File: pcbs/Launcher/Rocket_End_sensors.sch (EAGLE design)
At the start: 9 parts, among them U1 ARDUINO-MEGAPRO-5V, X1 22-23-2051, X3 22-23-2041, X5 22-23-2101, X6 22-23-2101, X7 22-23-2101, X8 22-23-2031

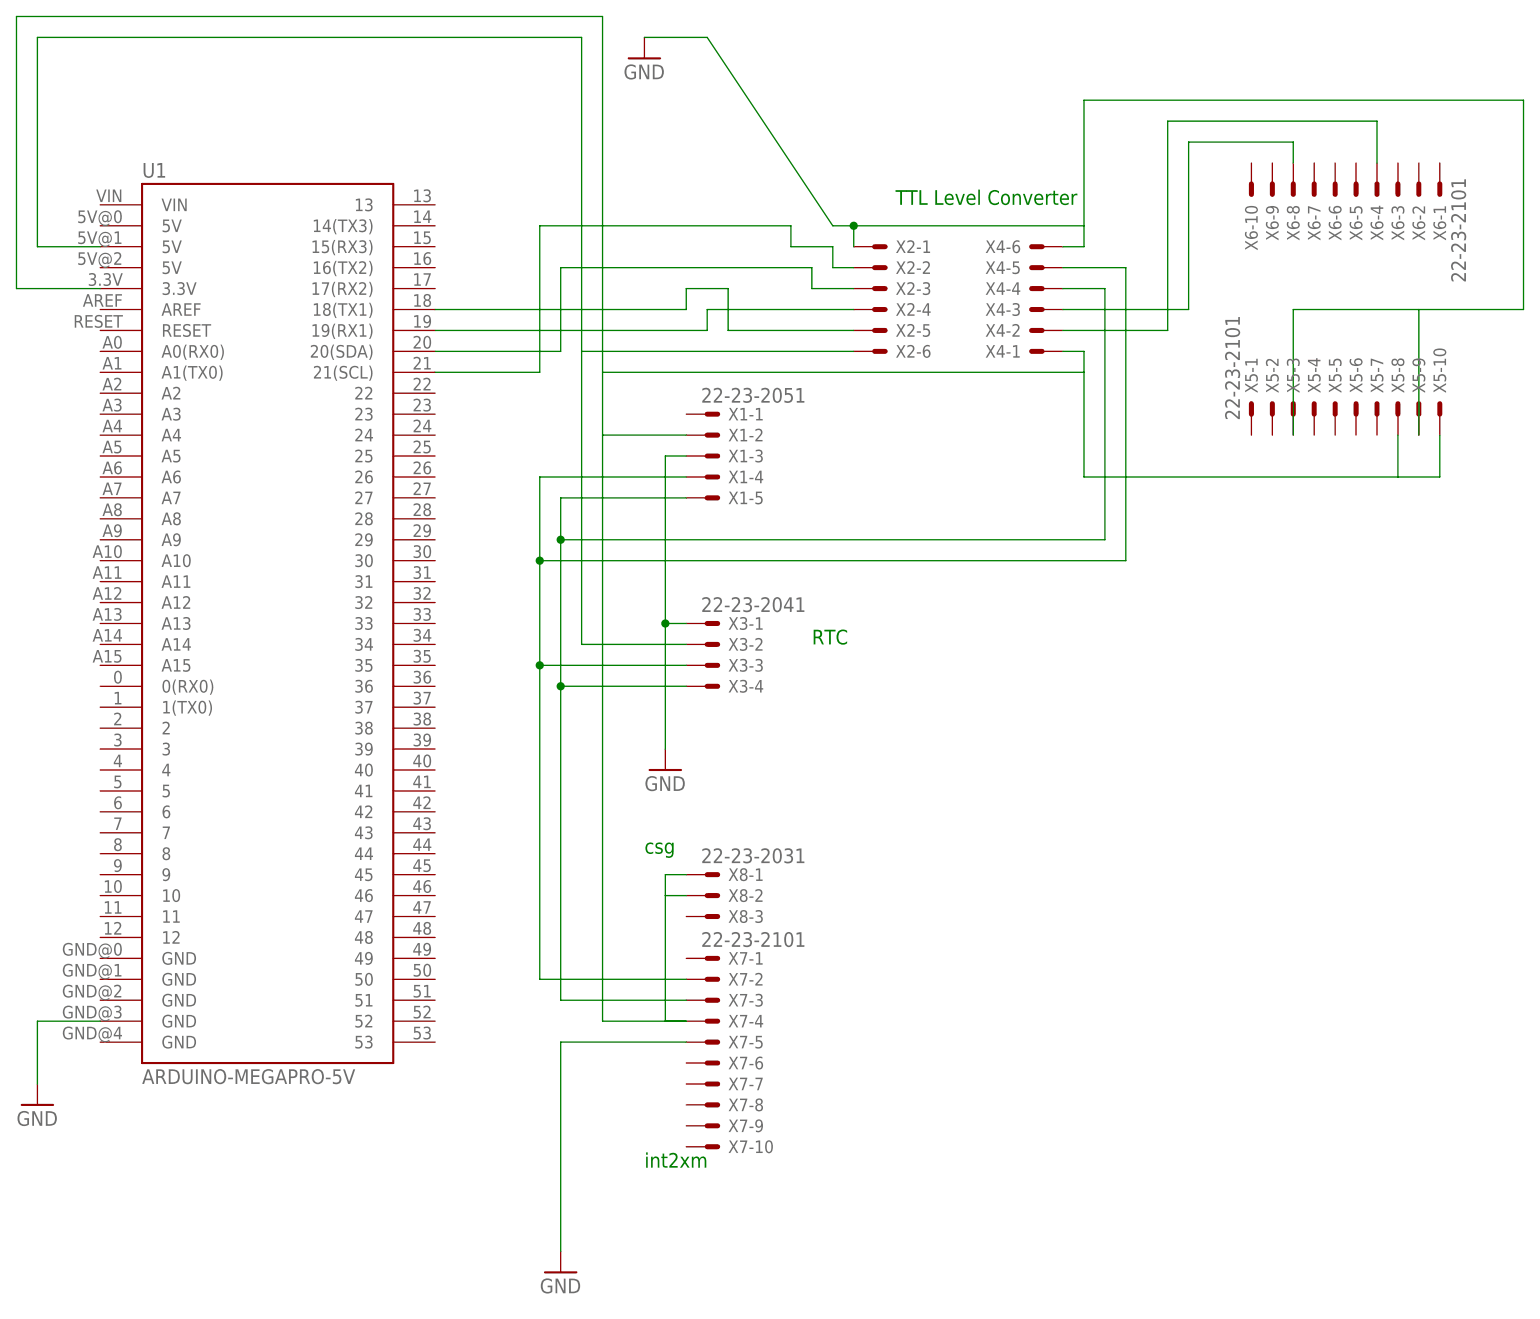
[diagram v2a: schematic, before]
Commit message: * More mods....fixed up gps wiring. * Making place where can run some wires underneath so don't need   two sides for relay board.
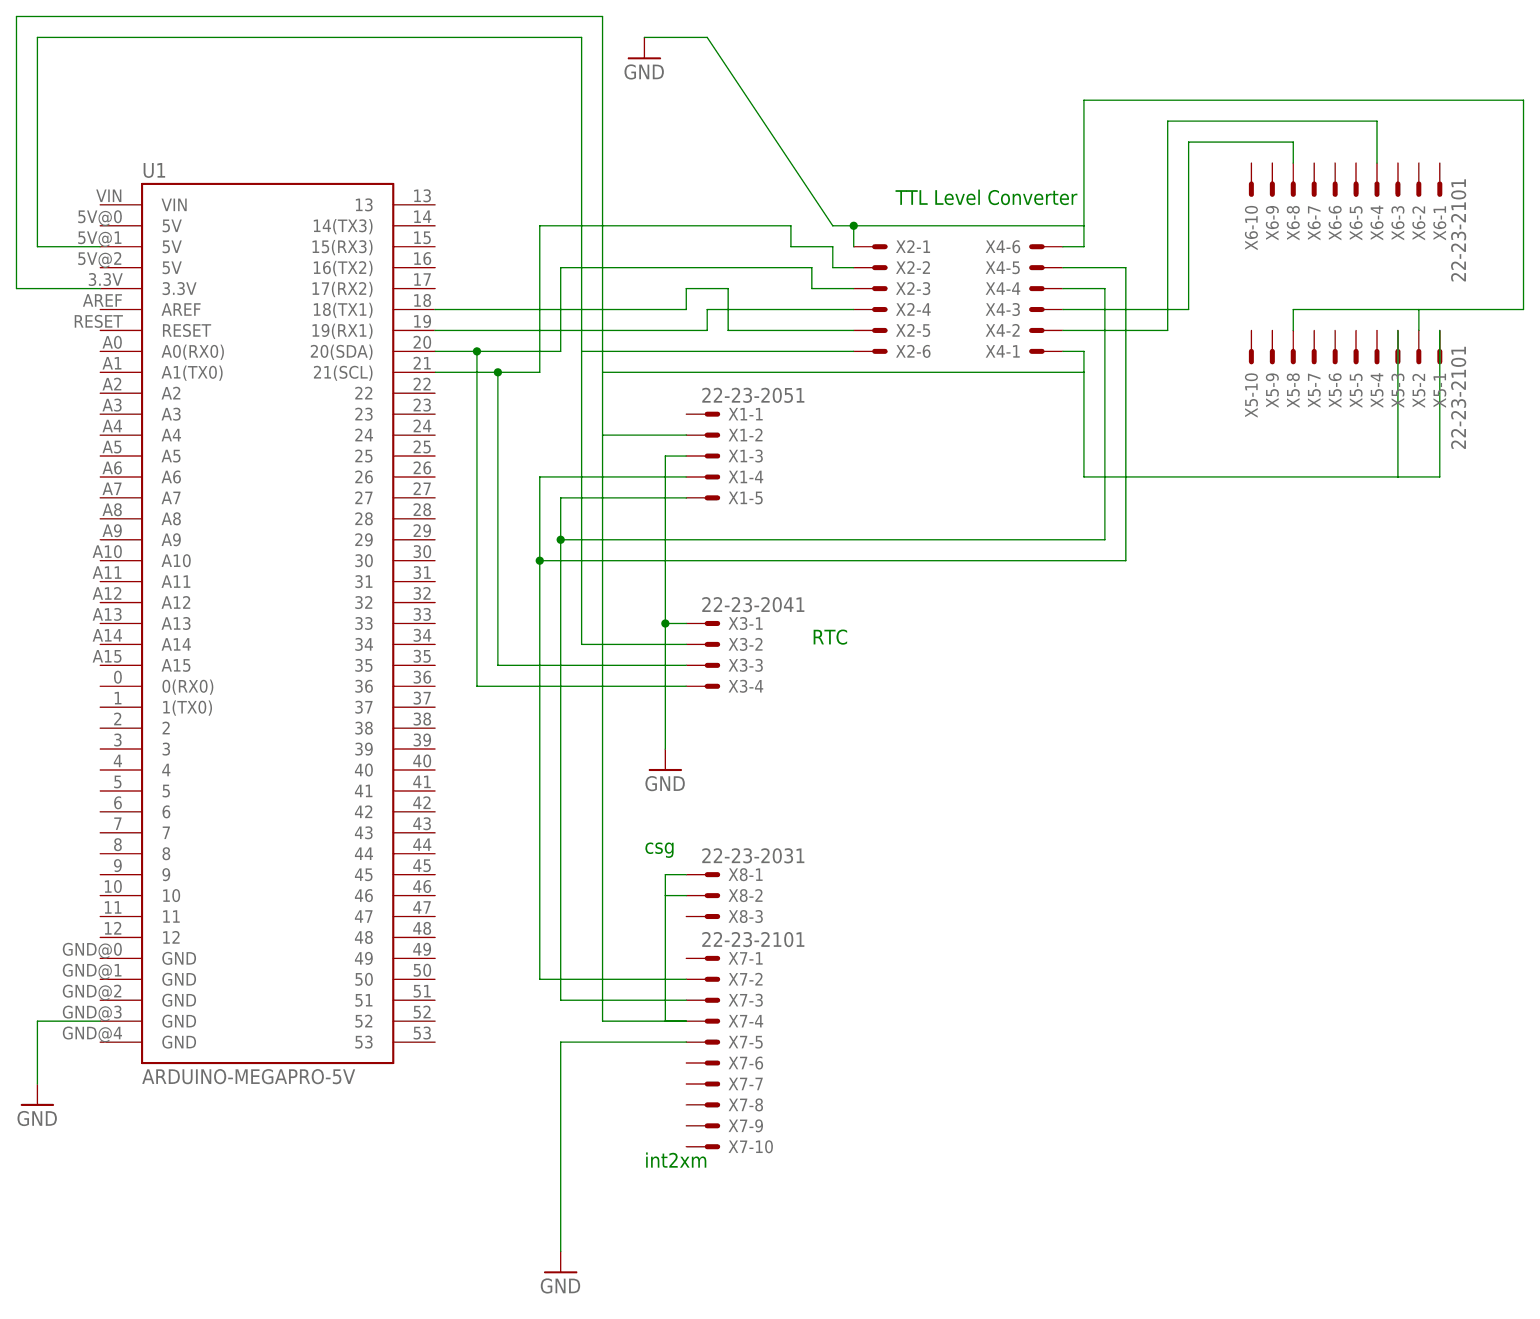
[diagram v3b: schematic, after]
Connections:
- net N$18: no longer X3-4.S
- net N$2: now also X3-3.S
- net N$24: no longer X3-3.S
- net N$4: now also X5-1.S, X5-3.S; no longer X5-10.S, X5-8.S
- net N$5: now also X3-4.S
- net N$7: now also X5-2.S, X5-8.S; no longer X5-3.S, X5-9.S
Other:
- moved on the sheet: X5-1, X5-10, X5-2, X5-3, X5-4, X5-5, X5-6, X5-7, X5-8, X5-9
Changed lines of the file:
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@@
 <part name="X4" library="con-molex" deviceset="22-23-2061" device=""/>
 <part name="GND2" library="supply1" deviceset="GND" device=""/>
-<part name="X5" library="con-molex" deviceset="22-23-2101" device=""/>
 <part name="X6" library="con-molex" deviceset="22-23-2101" device=""/>
 <part name="X7" library="con-molex" deviceset="22-23-2101" device=""/>
 <part name="X8" library="con-molex" deviceset="22-23-2031" device=""/>
 <part name="GND3" library="supply1" deviceset="GND" device=""/>
+<part name="X5" library="con-molex" deviceset="22-23-2101" device=""/>
 </parts>
 <sheets>
@@
 <instance part="X4" gate="-6" x="132.08" y="99.06" rot="R180"/>
 <instance part="GND2" gate="1" x="83.82" y="121.92"/>
-<instance part="X5" gate="-1" x="157.48" y="78.74" rot="R90"/>
-<instance part="X5" gate="-2" x="160.02" y="78.74" rot="R90"/>
-<instance part="X5" gate="-3" x="162.56" y="78.74" rot="R90"/>
-<instance part="X5" gate="-4" x="165.1" y="78.74" rot="R90"/>
-<instance part="X5" gate="-5" x="167.64" y="78.74" rot="R90"/>
-<instance part="X5" gate="-6" x="170.18" y="78.74" rot="R90"/>
-<instance part="X5" gate="-7" x="172.72" y="78.74" rot="R90"/>
-<instance part="X5" gate="-8" x="175.26" y="78.74" rot="R90"/>
-<instance part="X5" gate="-9" x="177.8" y="78.74" rot="R90"/>
-<instance part="X5" gate="-10" x="180.34" y="78.74" rot="R90"/>
 <instance part="X6" gate="-1" x="180.34" y="106.68" rot="R270"/>
 <instance part="X6" gate="-2" x="177.8" y="106.68" rot="R270"/>
@@
 <instance part="X8" gate="-3" x="91.44" y="17.78"/>
 <instance part="GND3" gate="1" x="73.66" y="-25.4"/>
+<instance part="X5" gate="-1" x="180.34" y="86.36" rot="R270"/>
+<instance part="X5" gate="-2" x="177.8" y="86.36" rot="R270"/>
+<instance part="X5" gate="-3" x="175.26" y="86.36" rot="R270"/>
+<instance part="X5" gate="-4" x="172.72" y="86.36" rot="R270"/>
+<instance part="X5" gate="-5" x="170.18" y="86.36" rot="R270"/>
+<instance part="X5" gate="-6" x="167.64" y="86.36" rot="R270"/>
+<instance part="X5" gate="-7" x="165.1" y="86.36" rot="R270"/>
+<instance part="X5" gate="-8" x="162.56" y="86.36" rot="R270"/>
+<instance part="X5" gate="-9" x="160.02" y="86.36" rot="R270"/>
+<instance part="X5" gate="-10" x="157.48" y="86.36" rot="R270"/>
 </instances>
 <busses>
@@
 <wire x1="88.9" y1="68.58" x2="73.66" y2="68.58" width="0.1524" layer="91"/>
 <pinref part="X7" gate="-3" pin="S"/>
-<wire x1="73.66" y1="63.5" x2="73.66" y2="45.72" width="0.1524" layer="91"/>
-<wire x1="73.66" y1="45.72" x2="73.66" y2="7.62" width="0.1524" layer="91"/>
+<wire x1="73.66" y1="63.5" x2="73.66" y2="7.62" width="0.1524" layer="91"/>
 <wire x1="73.66" y1="7.62" x2="88.9" y2="7.62" width="0.1524" layer="91"/>
 <wire x1="73.66" y1="63.5" x2="139.7" y2="63.5" width="0.1524" layer="91"/>
@@
 <wire x1="139.7" y1="93.98" x2="134.62" y2="93.98" width="0.1524" layer="91"/>
 <junction x="73.66" y="63.5"/>
-<pinref part="X3" gate="-4" pin="S"/>
-<wire x1="88.9" y1="45.72" x2="73.66" y2="45.72" width="0.1524" layer="91"/>
-<junction x="73.66" y="45.72"/>
 </segment>
 </net>
@@
 <wire x1="88.9" y1="71.12" x2="71.12" y2="71.12" width="0.1524" layer="91"/>
 <pinref part="X7" gate="-2" pin="S"/>
-<wire x1="71.12" y1="60.96" x2="71.12" y2="48.26" width="0.1524" layer="91"/>
-<wire x1="71.12" y1="48.26" x2="71.12" y2="10.16" width="0.1524" layer="91"/>
+<wire x1="71.12" y1="60.96" x2="71.12" y2="10.16" width="0.1524" layer="91"/>
 <wire x1="71.12" y1="10.16" x2="88.9" y2="10.16" width="0.1524" layer="91"/>
 <pinref part="X4" gate="-5" pin="S"/>
@@
 <wire x1="142.24" y1="60.96" x2="71.12" y2="60.96" width="0.1524" layer="91"/>
 <junction x="71.12" y="60.96"/>
-<pinref part="X3" gate="-3" pin="S"/>
-<wire x1="88.9" y1="48.26" x2="71.12" y2="48.26" width="0.1524" layer="91"/>
-<junction x="71.12" y="48.26"/>
 </segment>
 </net>
@@
 <net name="N$4" class="0">
 <segment>
-<pinref part="X5" gate="-10" pin="S"/>
-<wire x1="180.34" y1="76.2" x2="180.34" y2="71.12" width="0.1524" layer="91"/>
-<wire x1="180.34" y1="71.12" x2="175.26" y2="71.12" width="0.1524" layer="91"/>
-<pinref part="X5" gate="-8" pin="S"/>
-<wire x1="175.26" y1="71.12" x2="175.26" y2="76.2" width="0.1524" layer="91"/>
 <pinref part="X4" gate="-1" pin="S"/>
 <wire x1="137.16" y1="83.82" x2="137.16" y2="86.36" width="0.1524" layer="91"/>
@@
 <wire x1="17.78" y1="93.98" x2="7.62" y2="93.98" width="0.1524" layer="91"/>
 <wire x1="137.16" y1="83.82" x2="78.74" y2="83.82" width="0.1524" layer="91"/>
+<wire x1="180.34" y1="71.12" x2="175.26" y2="71.12" width="0.1524" layer="91"/>
 <wire x1="175.26" y1="71.12" x2="137.16" y2="71.12" width="0.1524" layer="91"/>
 <wire x1="137.16" y1="71.12" x2="137.16" y2="83.82" width="0.1524" layer="91"/>
@@
 <pinref part="X8" gate="-2" pin="S"/>
 <wire x1="88.9" y1="20.32" x2="86.36" y2="20.32" width="0.1524" layer="91"/>
+<pinref part="X5" gate="-1" pin="S"/>
+<wire x1="180.34" y1="71.12" x2="180.34" y2="88.9" width="0.1524" layer="91"/>
+<pinref part="X5" gate="-3" pin="S"/>
+<wire x1="175.26" y1="71.12" x2="175.26" y2="88.9" width="0.1524" layer="91"/>
 </segment>
 </net>
@@
 <segment>
 <pinref part="U1" gate="G$1" pin="21(SCL)"/>
-<wire x1="58.42" y1="83.82" x2="71.12" y2="83.82" width="0.1524" layer="91"/>
+<wire x1="58.42" y1="83.82" x2="66.04" y2="83.82" width="0.1524" layer="91"/>
+<wire x1="66.04" y1="83.82" x2="71.12" y2="83.82" width="0.1524" layer="91"/>
 <wire x1="71.12" y1="83.82" x2="71.12" y2="101.6" width="0.1524" layer="91"/>
 <wire x1="71.12" y1="101.6" x2="101.6" y2="101.6" width="0.1524" layer="91"/>
@@
 <pinref part="X2" gate="-2" pin="S"/>
 <wire x1="106.68" y1="96.52" x2="109.22" y2="96.52" width="0.1524" layer="91"/>
+<wire x1="66.04" y1="83.82" x2="66.04" y2="48.26" width="0.1524" layer="91"/>
+<pinref part="X3" gate="-3" pin="S"/>
+<wire x1="88.9" y1="48.26" x2="66.04" y2="48.26" width="0.1524" layer="91"/>
+<junction x="66.04" y="83.82"/>
 </segment>
 </net>
@@
 <segment>
 <pinref part="U1" gate="G$1" pin="20(SDA)"/>
-<wire x1="58.42" y1="86.36" x2="73.66" y2="86.36" width="0.1524" layer="91"/>
 <pinref part="X2" gate="-3" pin="S"/>
+<wire x1="63.5" y1="86.36" x2="73.66" y2="86.36" width="0.1524" layer="91"/>
 <wire x1="109.22" y1="93.98" x2="104.14" y2="93.98" width="0.1524" layer="91"/>
 <wire x1="104.14" y1="93.98" x2="104.14" y2="96.52" width="0.1524" layer="91"/>
 <wire x1="104.14" y1="96.52" x2="73.66" y2="96.52" width="0.1524" layer="91"/>
 <wire x1="73.66" y1="96.52" x2="73.66" y2="86.36" width="0.1524" layer="91"/>
+<wire x1="58.42" y1="86.36" x2="63.5" y2="86.36" width="0.1524" layer="91"/>
+<wire x1="63.5" y1="86.36" x2="63.5" y2="45.72" width="0.1524" layer="91"/>
+<pinref part="X3" gate="-4" pin="S"/>
+<wire x1="88.9" y1="45.72" x2="63.5" y2="45.72" width="0.1524" layer="91"/>
+<junction x="63.5" y="86.36"/>
 </segment>
 </net>
@@
 <wire x1="137.16" y1="101.6" x2="109.22" y2="101.6" width="0.1524" layer="91"/>
 <pinref part="X2" gate="-1" pin="S"/>
-<pinref part="X5" gate="-9" pin="S"/>
-<wire x1="177.8" y1="76.2" x2="177.8" y2="91.44" width="0.1524" layer="91"/>
+<wire x1="190.5" y1="91.44" x2="177.8" y2="91.44" width="0.1524" layer="91"/>
 <wire x1="177.8" y1="91.44" x2="162.56" y2="91.44" width="0.1524" layer="91"/>
-<pinref part="X5" gate="-3" pin="S"/>
-<wire x1="162.56" y1="91.44" x2="162.56" y2="76.2" width="0.1524" layer="91"/>
-<wire x1="177.8" y1="91.44" x2="190.5" y2="91.44" width="0.1524" layer="91"/>
 <wire x1="190.5" y1="91.44" x2="190.5" y2="116.84" width="0.1524" layer="91"/>
 <wire x1="190.5" y1="116.84" x2="137.16" y2="116.84" width="0.1524" layer="91"/>
@@
 <wire x1="109.22" y1="101.6" x2="106.68" y2="101.6" width="0.1524" layer="91"/>
 <junction x="109.22" y="101.6"/>
-</segment>
-</net>
+<pinref part="X5" gate="-2" pin="S"/>
+<wire x1="177.8" y1="88.9" x2="177.8" y2="91.44" width="0.1524" layer="91"/>
+<pinref part="X5" gate="-8" pin="S"/>
+<wire x1="162.56" y1="88.9" x2="162.56" y2="91.44" width="0.1524" layer="91"/>
+</segment>
+</net>
